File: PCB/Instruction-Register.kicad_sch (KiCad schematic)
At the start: 20 parts, among them U7 74LS245, U8 74LS173, U9 74LS173

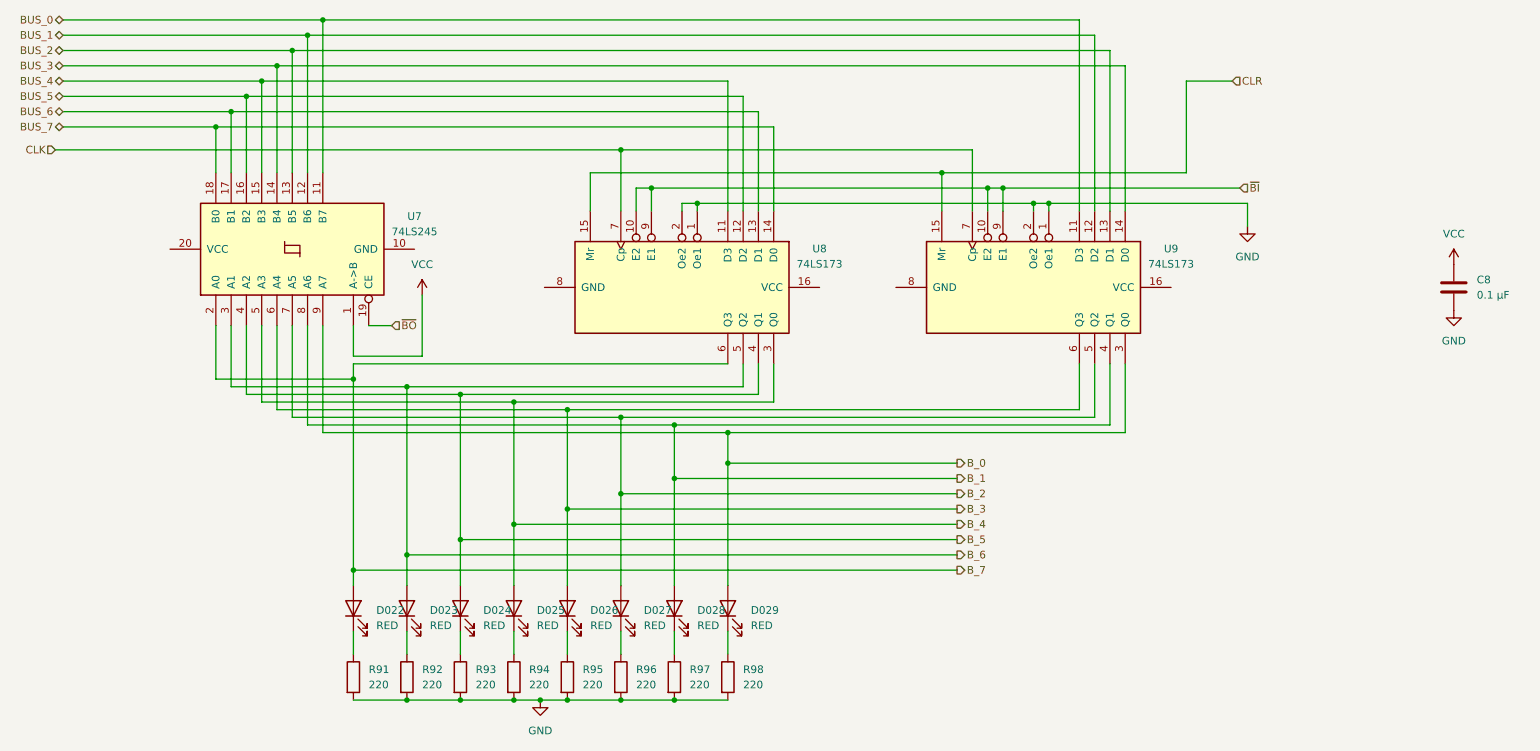
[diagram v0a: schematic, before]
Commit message: Cleaned up the schematic and got started on assigning all the footprints to the symbols
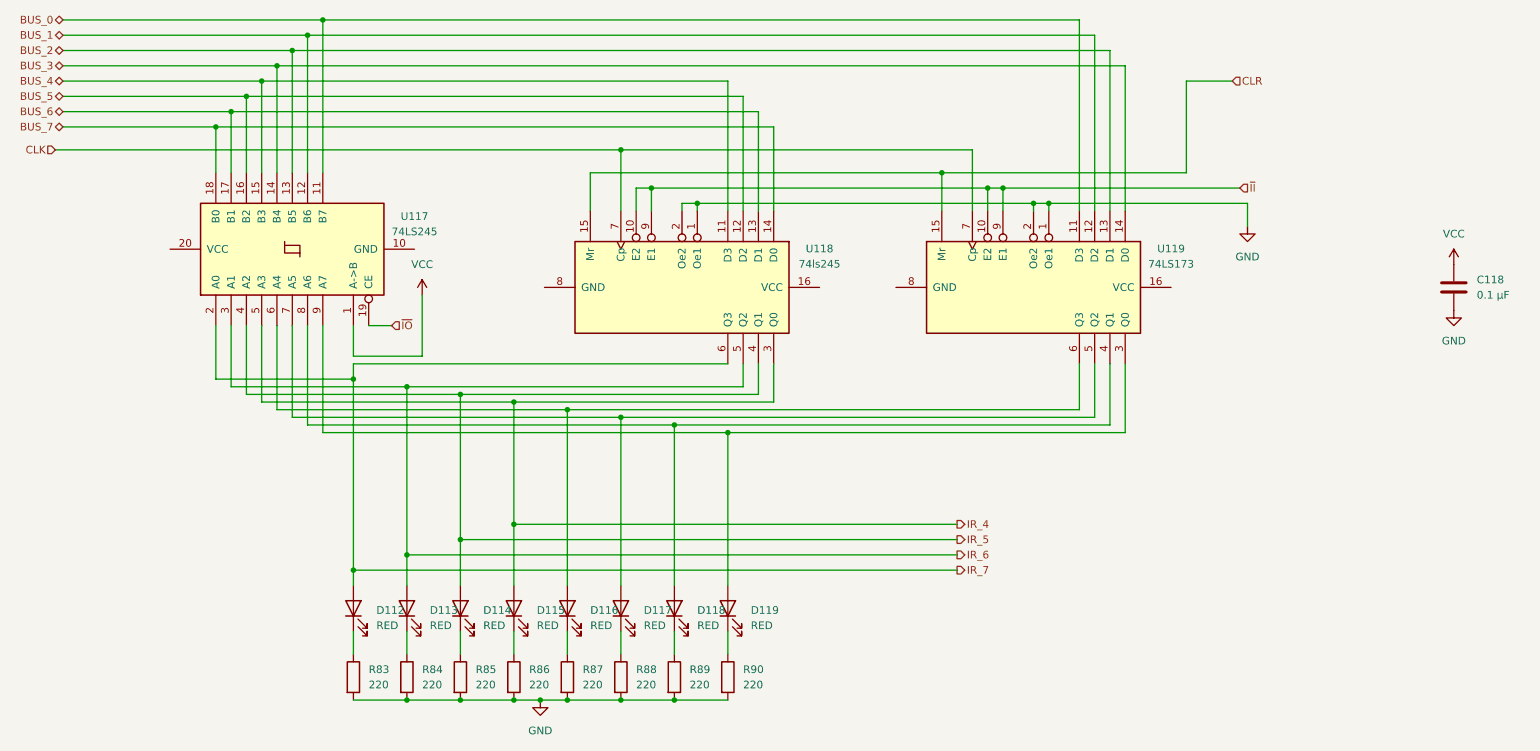
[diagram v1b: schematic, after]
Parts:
- removed C8: 0.1 µF, Capacitor_THT:C_Radial_D5.0mm_H5.0mm_P2.00mm, symbol Device:C
- removed D022, D023, D024, D025, D026, D027, D028, D029: RED, LED_THT:LED_D1.8mm_W1.8mm_H2.4mm_Horizontal_O1.27mm_Z1.6mm, symbol Device:LED
- removed R91, R92, R93, R94, R95, R96, R97, R98: 220, Resistor_THT:R_Axial_DIN0207_L6.3mm_D2.5mm_P7.62mm_Horizontal, symbol Device:R
- removed U7: 74LS245, symbol 74xx:74LS245
- removed U8, U9: 74LS173, symbol 74xx:74LS173
- added C118: 0.1 µF, Capacitor_THT:C_Radial_D5.0mm_H5.0mm_P2.00mm, symbol Device:C
- added D112, D113, D114, D115, D116, D117, D118, D119: RED, LED_THT:LED_D1.8mm_W1.8mm_H2.4mm_Horizontal_O1.27mm_Z1.6mm, symbol Device:LED
- added R83, R84, R85, R86, R87, R88, R89, R90: 220, Resistor_THT:R_Axial_DIN0207_L6.3mm_D2.5mm_P7.62mm_Horizontal, symbol Device:R
- added U117: 74LS245, symbol 74xx:74LS245
- added U118: 74ls245, symbol 74xx:74LS173
- added U119: 74LS173, symbol 74xx:74LS173
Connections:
- net BUS_0: now also U117.11 (B7), U119.11 (D3)
- net BUS_1: now also U117.12 (B6), U119.12 (D2)
- net BUS_2: now also U117.13 (B5), U119.13 (D1)
- net BUS_3: now also U117.14 (B4), U119.14 (D0)
- net BUS_4: now also U117.15 (B3), U118.11 (D3)
- net BUS_5: now also U117.16 (B2), U118.12 (D2)
- net BUS_6: now also U117.17 (B1), U118.13 (D1)
- net BUS_7: now also U117.18 (B0), U118.14 (D0)
- net CLK: now also U118.7 (Cp), U119.7 (Cp)
- net CLR: now also U118.15 (Mr), U119.15 (Mr)
- net GND: now also C118.2, R83.2, R84.2, R85.2, R86.2, R87.2, R88.2, R89.2, R90.2, U118.1 (Oe1), U118.2 (Oe2), U119.1 (Oe1), U119.2 (Oe2)
- net VCC: now also C118.1, U117.1 (A->B)
- new net: D118.1 (K), R89.1
- new net: D119.2 (A), U117.9 (A7), U119.3 (Q0)
- new net: D118.2 (A), U117.8 (A6), U119.4 (Q1)
- new net: D117.2 (A), U117.7 (A5), U119.5 (Q2)
- new net: D116.2 (A), U117.6 (A4), U119.6 (Q3)
- new net: D112.1 (K), R83.1
- new net: D115.1 (K), R86.1
- new net: D113.1 (K), R84.1
- new net: D117.1 (K), R88.1
- new net: D114.1 (K), R85.1
- new net: D119.1 (K), R90.1
- new net: D116.1 (K), R87.1
- new net IR_4: D115.2 (A), U117.5 (A3), U118.3 (Q0)
- new net IR_5: D114.2 (A), U117.4 (A2), U118.4 (Q1)
- new net IR_6: D113.2 (A), U117.3 (A1), U118.5 (Q2)
- new net IR_7: D112.2 (A), U117.2 (A0), U118.6 (Q3)
- new net ~{II}: U118.10 (E2), U118.9 (E1), U119.10 (E2), U119.9 (E1)
- new net ~{IO}: U117.19 (CE)

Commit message: added more models to work with on my pcb
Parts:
- D112, D113, D114, D115, D116, D117, D118, D119: footprint LED_THT:LED_D1.8mm_W1.8mm_H2.4mm_Horizontal_O1.27mm_Z1.6mm -> LED_THT:LED_D3.0mm
- U117, U118: footprint (none) -> Custom:DIP254P762X508-20
- U119: footprint (none) -> Custom:SN74LS173AN
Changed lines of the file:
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@@
 			)
 		)
-		(property "Footprint" ""
+		(property "Footprint" "Custom:SN74LS173AN"
 			(at 190.5 64.77 0)
 			(effects
@@
 			)
 		)
-		(property "Footprint" "LED_THT:LED_D1.8mm_W1.8mm_H2.4mm_Horizontal_O1.27mm_Z1.6mm"
+		(property "Footprint" "LED_THT:LED_D3.0mm"
 			(at 77.47 118.11 0)
 			(effects
@@
 			)
 		)
-		(property "Footprint" "LED_THT:LED_D1.8mm_W1.8mm_H2.4mm_Horizontal_O1.27mm_Z1.6mm"
+		(property "Footprint" "LED_THT:LED_D3.0mm"
 			(at 86.36 118.11 0)
 			(effects
@@
 			)
 		)
-		(property "Footprint" "LED_THT:LED_D1.8mm_W1.8mm_H2.4mm_Horizontal_O1.27mm_Z1.6mm"
+		(property "Footprint" "LED_THT:LED_D3.0mm"
 			(at 121.92 118.11 0)
 			(effects
@@
 			)
 		)
-		(property "Footprint" "LED_THT:LED_D1.8mm_W1.8mm_H2.4mm_Horizontal_O1.27mm_Z1.6mm"
+		(property "Footprint" "LED_THT:LED_D3.0mm"
 			(at 104.14 118.11 0)
 			(effects
@@
 			)
 		)
-		(property "Footprint" "LED_THT:LED_D1.8mm_W1.8mm_H2.4mm_Horizontal_O1.27mm_Z1.6mm"
+		(property "Footprint" "LED_THT:LED_D3.0mm"
 			(at 95.25 118.11 0)
 			(effects
@@
 			)
 		)
-		(property "Footprint" "LED_THT:LED_D1.8mm_W1.8mm_H2.4mm_Horizontal_O1.27mm_Z1.6mm"
+		(property "Footprint" "LED_THT:LED_D3.0mm"
 			(at 113.03 118.11 0)
 			(effects
@@
 			)
 		)
-		(property "Footprint" "LED_THT:LED_D1.8mm_W1.8mm_H2.4mm_Horizontal_O1.27mm_Z1.6mm"
+		(property "Footprint" "LED_THT:LED_D3.0mm"
 			(at 139.7 118.11 0)
 			(effects
@@
 			)
 		)
-		(property "Footprint" ""
+		(property "Footprint" "Custom:DIP254P762X508-20"
 			(at 132.08 64.77 0)
 			(effects
@@
 			)
 		)
-		(property "Footprint" "LED_THT:LED_D1.8mm_W1.8mm_H2.4mm_Horizontal_O1.27mm_Z1.6mm"
+		(property "Footprint" "LED_THT:LED_D3.0mm"
 			(at 130.81 118.11 0)
 			(effects
@@
 			)
 		)
-		(property "Footprint" ""
+		(property "Footprint" "Custom:DIP254P762X508-20"
 			(at 67.31 58.42 0)
 			(effects

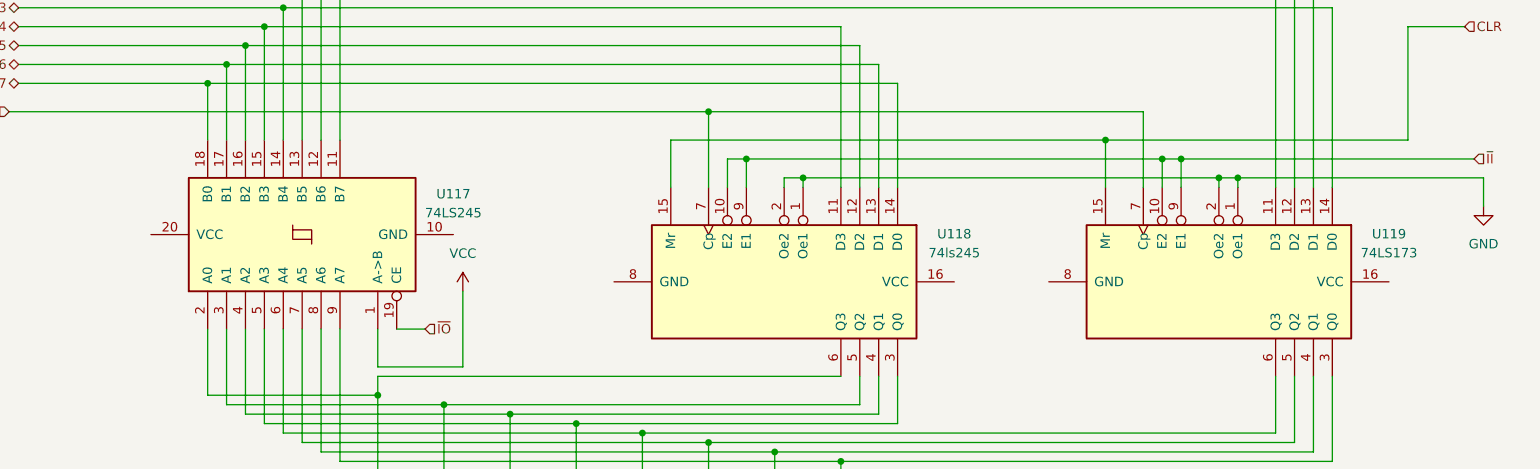
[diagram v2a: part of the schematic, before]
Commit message: got the PCB layed out into one group and started routing the traces and fixing DRC errors.
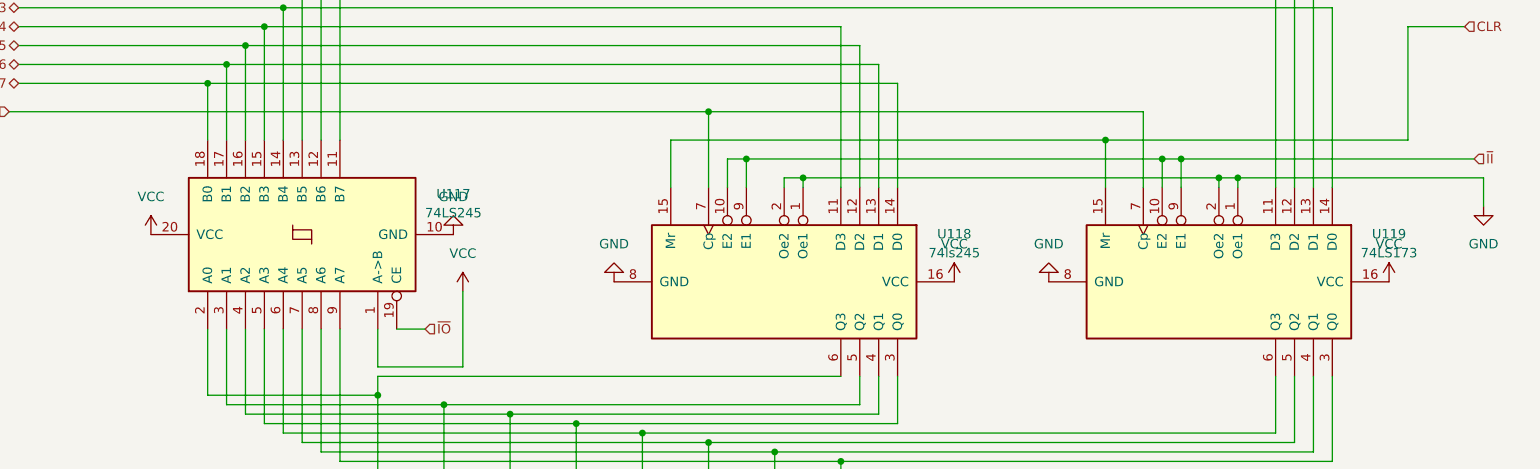
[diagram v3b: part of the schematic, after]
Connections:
- net GND: now also U117.10 (GND), U118.8 (GND), U119.8 (GND)
- net VCC: now also U117.20 (VCC), U118.16 (VCC), U119.16 (VCC)

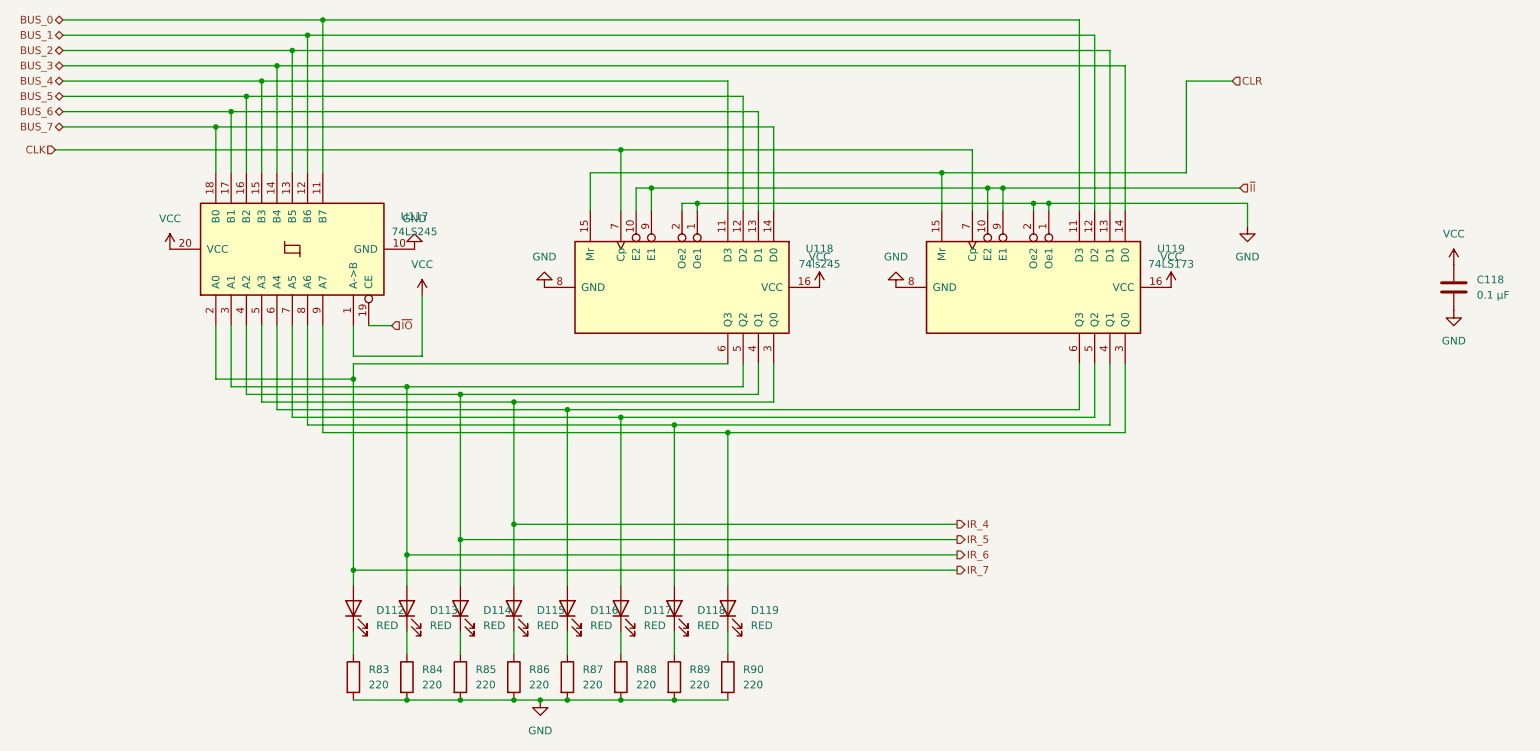
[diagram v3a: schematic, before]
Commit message: Fixed a bunch of ERC errors so know there is only one remaining.
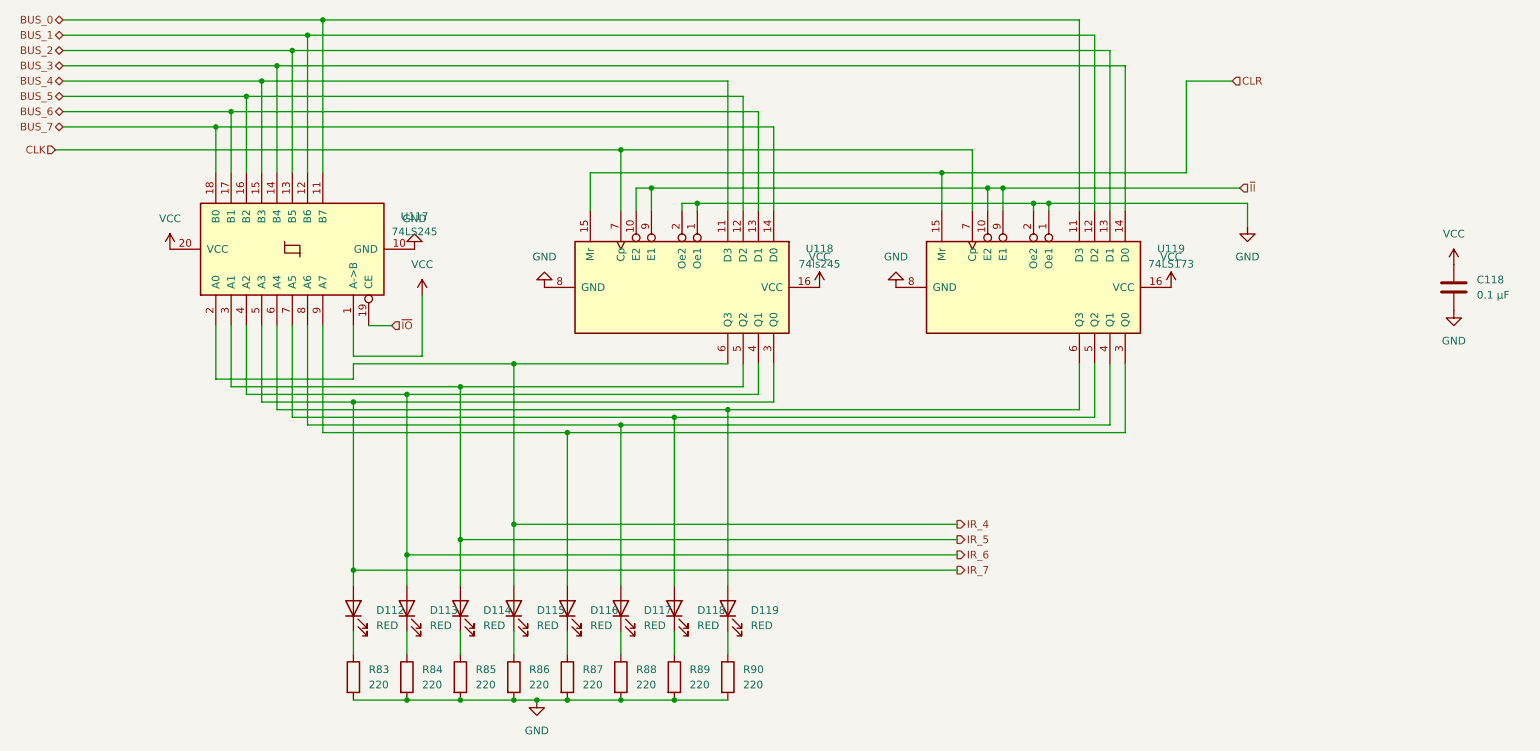
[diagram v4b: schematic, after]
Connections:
- net IR_4: now also U117.2 (A0), U118.6 (Q3); no longer U117.5 (A3), U118.3 (Q0)
- net IR_5: now also U117.3 (A1), U118.5 (Q2); no longer U117.4 (A2), U118.4 (Q1)
- net IR_6: now also U117.4 (A2), U118.4 (Q1); no longer U117.3 (A1), U118.5 (Q2)
- net IR_7: now also U117.5 (A3), U118.3 (Q0); no longer U117.2 (A0), U118.6 (Q3)
- net at U117.9 (A7), U119.3 (Q0): now also D116.2 (A); no longer D119.2 (A)
- net at U117.8 (A6), U119.4 (Q1): now also D117.2 (A); no longer D118.2 (A)
- net at U117.7 (A5), U119.5 (Q2): now also D118.2 (A); no longer D117.2 (A)
- net at U117.6 (A4), U119.6 (Q3): now also D119.2 (A); no longer D116.2 (A)

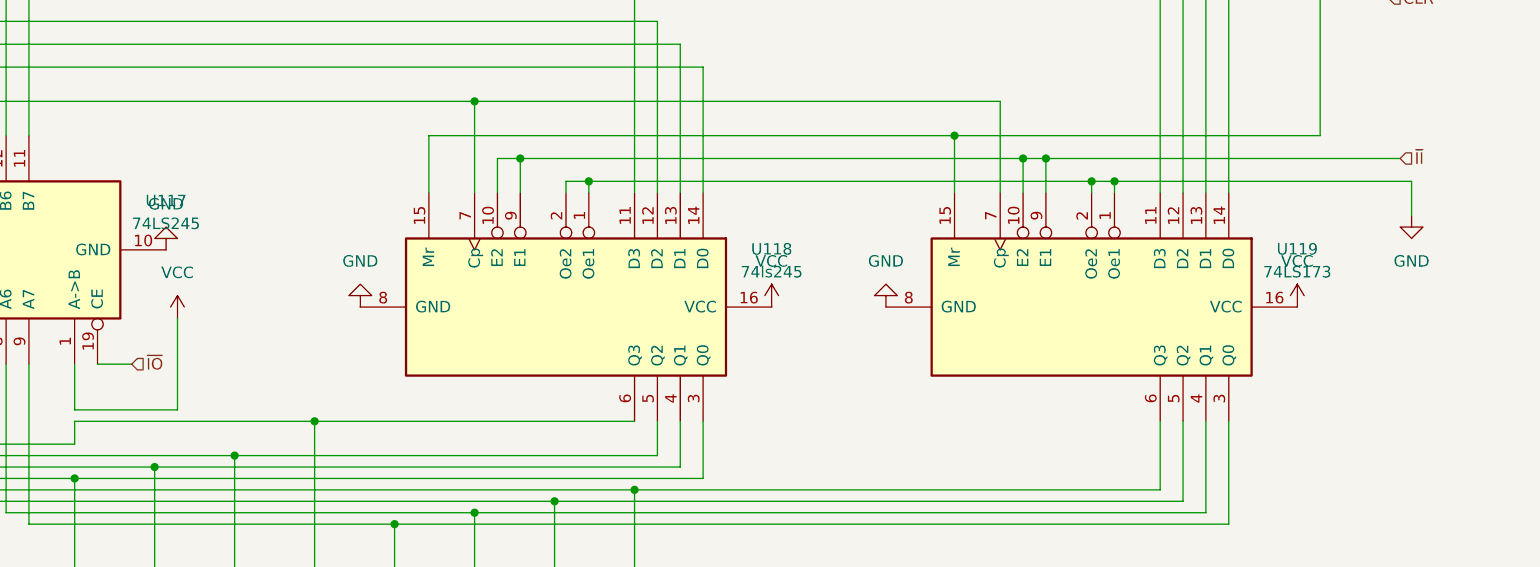
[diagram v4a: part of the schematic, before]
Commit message: Add decupling caps and reroute pcb. Updated BOM to match new number of caps
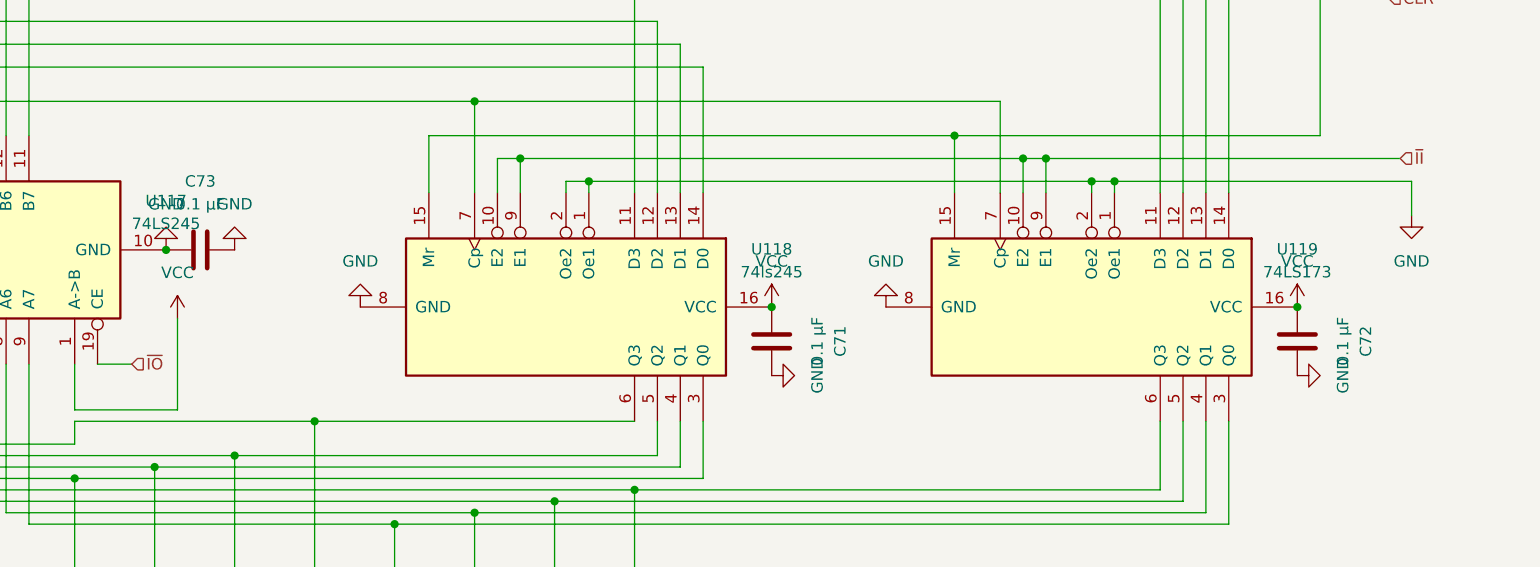
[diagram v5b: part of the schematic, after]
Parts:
- added C71, C72, C73: 0.1 µF, Capacitor_THT:C_Radial_D5.0mm_H5.0mm_P2.00mm, symbol Device:C
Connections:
- net GND: now also C71.2, C72.2, C73.1, C73.2
- net VCC: now also C71.1, C72.1
